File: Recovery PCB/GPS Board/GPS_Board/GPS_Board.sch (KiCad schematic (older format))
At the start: 11 parts, among them J1 XT30-M, J2 XT30-M, U1 Teensy4.1

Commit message: replace wires w labels
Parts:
- removed TP5: TestPoint, TestPoint:TestPoint_Pad_D1.0mm, symbol Connector:TestPoint
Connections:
- net labels added: AD2_SPI_CLOCK, AD3_SRI_CLOCK, AD3_SRI_SSEL, DTR, GPS_DTR, GPS_INT, GPS_PP5, ON_SLEEP, PCB_RESET, RSSL_PWM, SPI_MISO, SPI_MOSI
- wire segments 71 -> 48
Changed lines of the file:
@@
 	0    1    1    0
 $EndComp
-Wire Wire Line
-	4350 3600 4350 1600
-Wire Wire Line
-	4350 1600 4000 1600
 $Comp
 L power:GND #PWR0102
@@
 $EndComp
 Wire Wire Line
-	5300 3100 5300 2600
-Wire Wire Line
-	5300 2600 4000 2600
-Wire Wire Line
-	5350 2500 5350 3050
-Wire Wire Line
-	5350 3050 6475 3050
-Wire Wire Line
-	6475 3050 6475 3600
-Wire Wire Line
-	6475 3600 6425 3600
-Wire Wire Line
 	2900 4850 2950 4850
 Wire Wire Line
@@
 	1    0    0    -1
 $EndComp
-Wire Wire Line
-	5500 1425 4350 1425
-Wire Wire Line
-	4350 1425 4350 1600
-Connection ~ 4350 1600
-$Comp
-L Connector:TestPoint TP5
-U 1 1 61AB1BEF
-P 6150 1475
-F 0 "TP5" V 6104 1663 50  0000 L CNN
-F 1 "TestPoint" V 6195 1663 50  0000 L CNN
-F 2 "TestPoint:TestPoint_Pad_D1.0mm" H 6350 1475 50  0001 C CNN
-F 3 "~" H 6350 1475 50  0001 C CNN
-	1    6150 1475
-	0    1    1    0
-$EndComp
-Wire Wire Line
-	5500 1575 5300 1575
-Wire Wire Line
-	5300 1575 5300 750
-Wire Wire Line
-	5300 750  1250 750
-Wire Wire Line
-	1250 750  1250 2700
-Wire Wire Line
-	1250 2700 1800 2700
-Wire Wire Line
-	5500 1675 4175 1675
-Wire Wire Line
-	4175 1675 4175 1800
-Wire Wire Line
-	4175 1800 4000 1800
-Wire Wire Line
-	5500 1625 4775 1625
-Wire Wire Line
-	4775 1625 4775 3300
-Wire Wire Line
-	4775 3300 4000 3300
-Wire Wire Line
-	5500 1825 5375 1825
-Wire Wire Line
-	5375 1825 5375 3200
-Wire Wire Line
-	5375 3200 4000 3200
-Wire Wire Line
-	1800 2500 1475 2500
-Wire Wire Line
-	1475 2500 1475 950
-Wire Wire Line
-	1475 950  6500 950
-Wire Wire Line
-	6500 950  6500 1575
-Wire Wire Line
-	6500 1575 6150 1575
-Wire Wire Line
-	6150 1525 6425 1525
-Wire Wire Line
-	6425 1525 6425 1075
-Wire Wire Line
-	6425 1075 4550 1075
-Wire Wire Line
-	4550 1075 4550 2700
-Wire Wire Line
-	4550 2700 4000 2700
-Wire Wire Line
-	4525 2925 4525 3700
-Wire Wire Line
-	4525 3700 4000 3700
-Text GLabel 6225 1875 2    50   Input ~ 0
-MOSI
-Wire Wire Line
-	6150 1875 6225 1875
-Wire Wire Line
-	6150 1775 6525 1775
-Wire Wire Line
-	4525 2925 6525 2925
-Wire Wire Line
-	6525 1775 6525 2925
 Text GLabel 1725 2600 0    50   Input ~ 0
 MOSI
@@
 	0    -1   -1   0
 $EndComp
-Wire Wire Line
-	6425 3500 6425 3100
-Wire Wire Line
-	6425 3100 5300 3100
 Text GLabel 5600 5400 0    50   Input ~ 0
 bruh
@@
 Wire Wire Line
 	4000 3400 4440 3400
-Text Label 6850 3550 2    50   ~ 0
+Text Label 6750 3550 2    39   ~ 0
 GPS_RESET
 Wire Wire Line
 	6425 3550 6850 3550
+Wire Wire Line
+	6425 3600 6850 3600
+Text Label 4300 2500 2    50   ~ 0
+GPS_PP5
+Wire Wire Line
+	4000 2500 4300 2500
+Text Label 6850 3600 2    39   ~ 0
+GPS_PP5
+Wire Wire Line
+	6425 3500 6825 3500
+Wire Wire Line
+	4000 2600 4300 2600
+Text Label 4300 2600 2    50   ~ 0
+GPS_INT
+Text Label 6825 3500 2    39   ~ 0
+GPS_INT
+Text Label 4450 2700 2    39   ~ 0
+AD2_SPI_CLOCK
+Wire Wire Line
+	4000 2700 4450 2700
+Text Label 6625 1525 2    39   ~ 0
+AD2_SPI_CLOCK
+Wire Wire Line
+	6150 1525 6625 1525
+Wire Wire Line
+	6150 1575 6625 1575
+Text Label 6625 1575 2    39   ~ 0
+AD3_SRI_SSEL
+Text Label 1400 2500 0    39   ~ 0
+AD3_SRI_CLOCK
+Wire Wire Line
+	1400 2500 1800 2500
+$Comp
+L power:+3.3V #PWR?
+U 1 1 625CE6B8
+P 5500 1425
+F 0 "#PWR?" H 5500 1275 50  0001 C CNN
+F 1 "+3.3V" H 5515 1598 50  0000 C CNN
+F 2 "" H 5500 1425 50  0001 C CNN
+F 3 "" H 5500 1425 50  0001 C CNN
+	1    5500 1425
+	1    0    0    -1
+$EndComp
+Text Label 5250 1575 0    39   ~ 0
+SPI_MISO
+Wire Wire Line
+	5250 1575 5500 1575
+Text Label 1525 2700 0    39   ~ 0
+SPI_MISO
+Wire Wire Line
+	1800 2700 1525 2700
+Wire Wire Line
+	5500 1625 5250 1625
+Wire Wire Line
+	4000 3300 4425 3300
+Text Label 4375 3300 2    39   ~ 0
+PCB_RESET
+Text Label 5250 1625 0    39   ~ 0
+PCB_RESET
+Wire Wire Line
+	5500 1675 5250 1675
+Text Label 5250 1675 0    39   ~ 0
+RSSL_PWM
+Wire Wire Line
+	4000 1800 4325 1800
+Text Label 4325 1800 2    39   ~ 0
+RSSL_PWM
+Wire Wire Line
+	5500 1825 5250 1825
+Text Label 5250 1825 0    39   ~ 0
+DTR
+Wire Wire Line
+	4000 3200 4400 3200
+Text Label 4400 3200 2    39   ~ 0
+GPS_DTR
+Wire Wire Line
+	6150 1775 6575 1775
+Text Label 6575 1775 2    39   ~ 0
+ON_SLEEP
+Wire Wire Line
+	4000 3700 4425 3700
+Text Label 4425 3700 2    39   ~ 0
+ON_SLEEP
+$Comp
+L power:+3.3V #PWR?
+U 1 1 625E340B
+P 4000 1600
+F 0 "#PWR?" H 4000 1450 50  0001 C CNN
+F 1 "+3.3V" V 4015 1728 50  0000 L CNN
+F 2 "" H 4000 1600 50  0001 C CNN
+F 3 "" H 4000 1600 50  0001 C CNN
+	1    4000 1600
+	0    1    1    0
+$EndComp
+Wire Wire Line
+	6150 1875 6575 1875
+Text Label 6575 1875 2    39   ~ 0
+SPI_MOSI
 $EndSCHEMATC

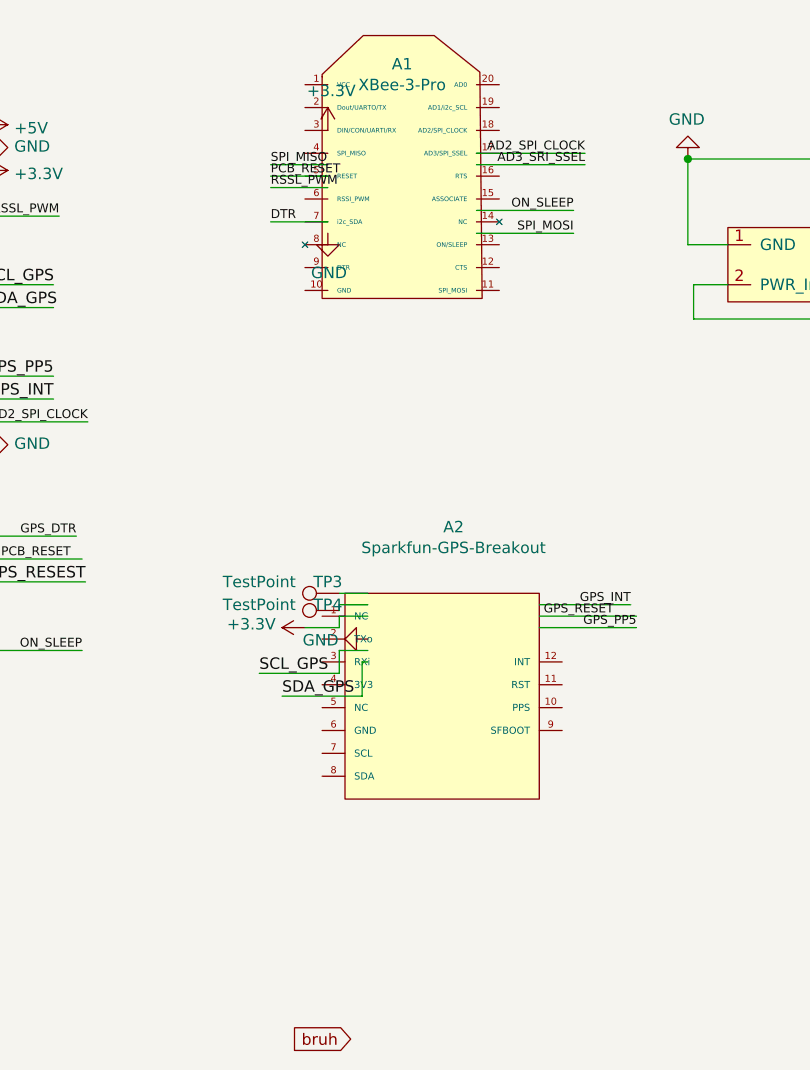
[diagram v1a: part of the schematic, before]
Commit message: Updated Xbee Symbol and font
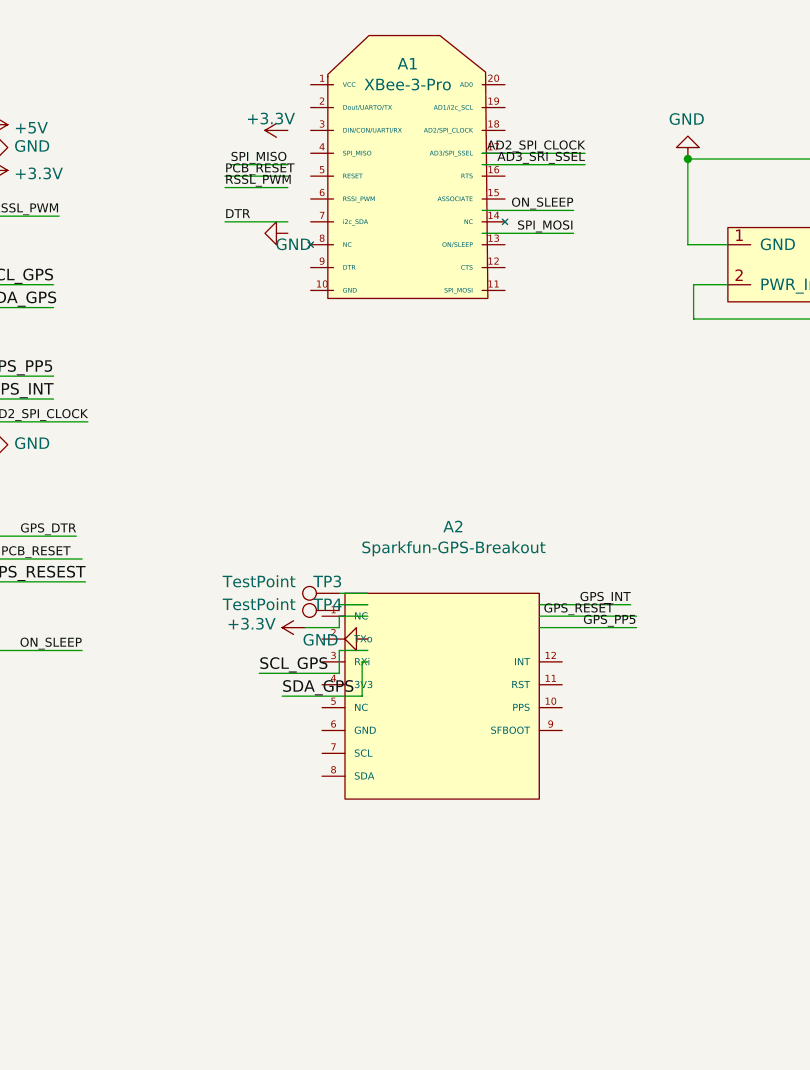
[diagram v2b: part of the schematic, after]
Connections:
- net labels removed: bruh
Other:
- moved on the sheet: A1
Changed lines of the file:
@@
-$EndComp
-$Comp
-L GPS_Board:XBee-3-Pro A1
-U 1 1 61AB64FA
-P 5825 1900
-F 0 "A1" H 5825 2665 50  0000 C CNN
-F 1 "XBee-3-Pro" H 5825 2574 50  0000 C CNN
-F 2 "GPS Board:XBEE-20_THT" H 5825 1900 50  0001 C CNN
-F 3 "" H 5825 1900 50  0001 C CNN
-	1    5825 1900
-	1    0    0    -1
 $EndComp
 $Comp
@@
 L power:GND #PWR0106
 U 1 1 61ACAD1F
-P 5500 1875
-F 0 "#PWR0106" H 5500 1625 50  0001 C CNN
-F 1 "GND" H 5505 1702 50  0000 C CNN
-F 2 "" H 5500 1875 50  0001 C CNN
-F 3 "" H 5500 1875 50  0001 C CNN
-	1    5500 1875
-	1    0    0    -1
+P 5325 1875
+F 0 "#PWR0106" H 5325 1625 50  0001 C CNN
+F 1 "GND" V 5375 1900 50  0000 C CNN
+F 2 "" H 5325 1875 50  0001 C CNN
+F 3 "" H 5325 1875 50  0001 C CNN
+	1    5325 1875
+	0    1    1    0
 $EndComp
 $Comp
@@
 	0    -1   -1   0
 $EndComp
-Text GLabel 5600 5400 0    50   Input ~ 0
-bruh
 Text Label 4440 3400 2    50   ~ 0
 GPS_RESEST
@@
 Text Label 6625 1525 2    39   ~ 0
 AD2_SPI_CLOCK
-Wire Wire Line
-	6150 1525 6625 1525
-Wire Wire Line
-	6150 1575 6625 1575
 Text Label 6625 1575 2    39   ~ 0
 AD3_SRI_SSEL
@@
 L power:+3.3V #PWR?
 U 1 1 625CE6B8
-P 5500 1425
-F 0 "#PWR?" H 5500 1275 50  0001 C CNN
-F 1 "+3.3V" H 5515 1598 50  0000 C CNN
-F 2 "" H 5500 1425 50  0001 C CNN
-F 3 "" H 5500 1425 50  0001 C CNN
-	1    5500 1425
-	1    0    0    -1
-$EndComp
-Text Label 5250 1575 0    39   ~ 0
+P 5325 1425
+F 0 "#PWR?" H 5325 1275 50  0001 C CNN
+F 1 "+3.3V" V 5375 1500 50  0000 C CNN
+F 2 "" H 5325 1425 50  0001 C CNN
+F 3 "" H 5325 1425 50  0001 C CNN
+	1    5325 1425
+	0    -1   -1   0
+$EndComp
+Text Label 5075 1575 0    39   ~ 0
 SPI_MISO
-Wire Wire Line
-	5250 1575 5500 1575
 Text Label 1525 2700 0    39   ~ 0
 SPI_MISO
 Wire Wire Line
 	1800 2700 1525 2700
-Wire Wire Line
-	5500 1625 5250 1625
 Wire Wire Line
 	4000 3300 4425 3300
 Text Label 4375 3300 2    39   ~ 0
 PCB_RESET
-Text Label 5250 1625 0    39   ~ 0
+Text Label 5050 1625 0    39   ~ 0
 PCB_RESET
-Wire Wire Line
-	5500 1675 5250 1675
-Text Label 5250 1675 0    39   ~ 0
+Text Label 5050 1675 0    39   ~ 0
 RSSL_PWM
 Wire Wire Line
@@
 Text Label 4325 1800 2    39   ~ 0
 RSSL_PWM
-Wire Wire Line
-	5500 1825 5250 1825
-Text Label 5250 1825 0    39   ~ 0
+Text Label 5050 1825 0    39   ~ 0
 DTR
 Wire Wire Line
@@
 Text Label 4400 3200 2    39   ~ 0
 GPS_DTR
-Wire Wire Line
-	6150 1775 6575 1775
 Text Label 6575 1775 2    39   ~ 0
 ON_SLEEP
@@
 	0    1    1    0
 $EndComp
-Wire Wire Line
-	6150 1875 6575 1875
 Text Label 6575 1875 2    39   ~ 0
 SPI_MOSI
+Wire Wire Line
+	6175 1525 6625 1525
+Wire Wire Line
+	6175 1575 6625 1575
+Wire Wire Line
+	6175 1775 6575 1775
+Wire Wire Line
+	6175 1875 6575 1875
+Wire Wire Line
+	5325 1825 5050 1825
+Wire Wire Line
+	5325 1675 5050 1675
+Wire Wire Line
+	5325 1625 5050 1625
+$Comp
+L GPS_Board:XBee-3-Pro A1
+U 1 1 61AB64FA
+P 5850 1900
+F 0 "A1" H 5850 2665 50  0000 C CNN
+F 1 "XBee-3-Pro" H 5850 2574 50  0000 C CNN
+F 2 "GPS Board:XBEE-20_THT" H 5850 1900 50  0001 C CNN
+F 3 "" H 5850 1900 50  0001 C CNN
+	1    5850 1900
+	1    0    0    -1
+$EndComp
+Wire Wire Line
+	5075 1575 5325 1575
 $EndSCHEMATC

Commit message: Changed some labels
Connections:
- net labels added: GPS_SCL, GPS_SDA, XBee_CS, XBee_DTR, XBee_MISO, XBee_MOSI, XBee_PWM, XBee_RESET, XBee_Reset, XBee_SCK
- net labels removed: AD2_SPI_CLOCK, AD3_SRI_CLOCK, AD3_SRI_SSEL, DTR, GPS_DTR, MOSI, PCB_RESET, RSSL_PWM, SCL_GPS, SDA_GPS, SPI_MISO, SPI_MOSI
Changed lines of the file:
@@
 	1    0    0    -1
 $EndComp
-Text GLabel 1725 2600 0    50   Input ~ 0
-MOSI
-Wire Wire Line
-	1800 2600 1725 2600
 $Comp
 L power:GND #PWR?
@@
 	5650 3750 5675 3750
 Text Label 4000 2100 0    50   ~ 0
-SCL_GPS
+GPS_SCL
 Text Label 4000 2200 0    50   ~ 0
-SDA_GPS
+GPS_SDA
 Text Label 5200 3800 0    50   ~ 0
-SCL_GPS
+GPS_SCL
 Text Label 5300 3900 0    50   ~ 0
-SDA_GPS
+GPS_SDA
 Wire Wire Line
 	4000 2100 4300 2100
@@
 GPS_INT
 Text Label 4450 2700 2    39   ~ 0
-AD2_SPI_CLOCK
+XBee_SCK
 Wire Wire Line
 	4000 2700 4450 2700
 Text Label 6625 1525 2    39   ~ 0
-AD2_SPI_CLOCK
-Text Label 6625 1575 2    39   ~ 0
-AD3_SRI_SSEL
+XBee_SCK
 Text Label 1400 2500 0    39   ~ 0
-AD3_SRI_CLOCK
+XBee_CS
 Wire Wire Line
 	1400 2500 1800 2500
@@
 	0    -1   -1   0
 $EndComp
-Text Label 5075 1575 0    39   ~ 0
-SPI_MISO
 Text Label 1525 2700 0    39   ~ 0
-SPI_MISO
+XBee_MISO
 Wire Wire Line
 	1800 2700 1525 2700
@@
 	4000 3300 4425 3300
 Text Label 4375 3300 2    39   ~ 0
-PCB_RESET
-Text Label 5050 1625 0    39   ~ 0
-PCB_RESET
+XBee_RESET
 Text Label 5050 1675 0    39   ~ 0
-RSSL_PWM
+XBee_PWM
 Wire Wire Line
 	4000 1800 4325 1800
 Text Label 4325 1800 2    39   ~ 0
-RSSL_PWM
+XBee_PWM
 Text Label 5050 1825 0    39   ~ 0
-DTR
+XBee_DTR
 Wire Wire Line
 	4000 3200 4400 3200
 Text Label 4400 3200 2    39   ~ 0
-GPS_DTR
+XBee_DTR
 Text Label 6575 1775 2    39   ~ 0
 ON_SLEEP
@@
 $EndComp
 Text Label 6575 1875 2    39   ~ 0
-SPI_MOSI
+XBee_MOSI
 Wire Wire Line
 	6175 1525 6625 1525
@@
 $EndComp
 Wire Wire Line
-	5075 1575 5325 1575
+	1800 2600 1525 2600
+Text Label 1525 2600 0    39   ~ 0
+XBee_MOSI
+Text Label 6625 1575 2    39   ~ 0
+XBee_CS
+Text Label 5050 1625 0    39   ~ 0
+XBee_Reset
+Text Label 5050 1575 0    39   ~ 0
+XBee_MISO
+Wire Wire Line
+	5050 1575 5325 1575
 $EndSCHEMATC

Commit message: Adjusted XBEE labels, and symbol
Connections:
- net labels added: XBEE_SCL, XBEE_SDA
- wire segments 48 -> 52
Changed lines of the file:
@@
 L power:GND #PWR0106
 U 1 1 61ACAD1F
-P 5325 1875
-F 0 "#PWR0106" H 5325 1625 50  0001 C CNN
-F 1 "GND" V 5375 1900 50  0000 C CNN
-F 2 "" H 5325 1875 50  0001 C CNN
-F 3 "" H 5325 1875 50  0001 C CNN
-	1    5325 1875
+P 5425 2125
+F 0 "#PWR0106" H 5425 1875 50  0001 C CNN
+F 1 "GND" V 5425 1950 50  0000 C CNN
+F 2 "" H 5425 2125 50  0001 C CNN
+F 3 "" H 5425 2125 50  0001 C CNN
+	1    5425 2125
 	0    1    1    0
 $EndComp
@@
 Text Label 6825 3500 2    39   ~ 0
 GPS_INT
-Text Label 4450 2700 2    39   ~ 0
+Text Label 4325 2700 2    39   ~ 0
 XBee_SCK
 Wire Wire Line
-	4000 2700 4450 2700
-Text Label 6625 1525 2    39   ~ 0
+	4000 2700 4325 2700
+Text Label 6575 1425 2    39   ~ 0
 XBee_SCK
 Text Label 1400 2500 0    39   ~ 0
@@
 L power:+3.3V #PWR?
 U 1 1 625CE6B8
-P 5325 1425
-F 0 "#PWR?" H 5325 1275 50  0001 C CNN
-F 1 "+3.3V" V 5375 1500 50  0000 C CNN
-F 2 "" H 5325 1425 50  0001 C CNN
-F 3 "" H 5325 1425 50  0001 C CNN
-	1    5325 1425
+P 5425 1225
+F 0 "#PWR?" H 5425 1075 50  0001 C CNN
+F 1 "+3.3V" V 5475 1300 50  0000 C CNN
+F 2 "" H 5425 1225 50  0001 C CNN
+F 3 "" H 5425 1225 50  0001 C CNN
+	1    5425 1225
 	0    -1   -1   0
 $EndComp
@@
 Text Label 4375 3300 2    39   ~ 0
 XBee_RESET
-Text Label 5050 1675 0    39   ~ 0
+Text Label 5150 1725 0    39   ~ 0
 XBee_PWM
 Wire Wire Line
@@
 Text Label 4325 1800 2    39   ~ 0
 XBee_PWM
-Text Label 5050 1825 0    39   ~ 0
+Text Label 5150 2025 0    39   ~ 0
 XBee_DTR
 Wire Wire Line
@@
 Text Label 4400 3200 2    39   ~ 0
 XBee_DTR
-Text Label 6575 1775 2    39   ~ 0
+Text Label 6675 1925 2    39   ~ 0
 ON_SLEEP
 Wire Wire Line
@@
 	0    1    1    0
 $EndComp
-Text Label 6575 1875 2    39   ~ 0
+Text Label 6675 2125 2    39   ~ 0
 XBee_MOSI
 Wire Wire Line
-	6175 1525 6625 1525
-Wire Wire Line
-	6175 1575 6625 1575
-Wire Wire Line
-	6175 1775 6575 1775
-Wire Wire Line
-	6175 1875 6575 1875
-Wire Wire Line
-	5325 1825 5050 1825
-Wire Wire Line
-	5325 1675 5050 1675
-Wire Wire Line
-	5325 1625 5050 1625
+	6275 1525 6575 1525
+Wire Wire Line
+	6275 1925 6675 1925
+Wire Wire Line
+	6275 2125 6675 2125
+Wire Wire Line
+	5425 2025 5150 2025
+Wire Wire Line
+	5425 1725 5150 1725
+Wire Wire Line
+	5425 1625 5150 1625
 $Comp
 L GPS_Board:XBee-3-Pro A1
 U 1 1 61AB64FA
 P 5850 1900
-F 0 "A1" H 5850 2665 50  0000 C CNN
-F 1 "XBee-3-Pro" H 5850 2574 50  0000 C CNN
+F 0 "A1" H 5850 2750 50  0000 C CNN
+F 1 "XBee-3-Pro" H 5850 2675 50  0000 C CNN
 F 2 "GPS Board:XBEE-20_THT" H 5850 1900 50  0001 C CNN
 F 3 "" H 5850 1900 50  0001 C CNN
@@
 Text Label 1525 2600 0    39   ~ 0
 XBee_MOSI
-Text Label 6625 1575 2    39   ~ 0
+Text Label 6575 1525 2    39   ~ 0
 XBee_CS
-Text Label 5050 1625 0    39   ~ 0
+Text Label 5150 1625 0    39   ~ 0
 XBee_Reset
-Text Label 5050 1575 0    39   ~ 0
+Text Label 5150 1525 0    39   ~ 0
 XBee_MISO
 Wire Wire Line
-	5050 1575 5325 1575
+	5150 1525 5425 1525
+Wire Wire Line
+	6275 1425 6575 1425
+Wire Wire Line
+	5150 1825 5425 1825
+Wire Wire Line
+	6275 1325 6575 1325
+Text Label 5150 1825 0    39   ~ 0
+XBEE_SDA
+Text Label 6575 1325 2    39   ~ 0
+XBEE_SCL
+Wire Wire Line
+	4000 2300 4300 2300
+Wire Wire Line
+	4000 2400 4300 2400
+Text Label 4300 2300 2    39   ~ 0
+XBEE_SDA
+Text Label 4300 2400 2    39   ~ 0
+XBEE_SCL
 $EndSCHEMATC
